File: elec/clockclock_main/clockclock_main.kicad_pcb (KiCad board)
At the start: 2 copper layers, 226.2 x 90.5 mm, 132 parts, among them J1 rotary_encoder, J2 DCF77 board, J3 RTC, J4 rotary_encoder, M1 Conn motor 0, M10 Conn motor 1, M11 Conn motor 0, M12 Conn motor 1, M13 Conn motor 0, M14 Conn motor 1, M15 Conn motor 0, M16 Conn motor 1, M17 Conn motor 0, M18 Conn motor 1, M19 Conn motor 0, M2 Conn motor 1, M20 Conn motor 1, M21 Conn motor 0, M22 Conn motor 1, M23 Conn motor 0, M24 Conn motor 1, M3 Conn motor 0, M4 Conn motor 1, M5 Conn motor 0, M6 Conn motor 1, M7 Conn motor 0, M8 Conn motor 1, M9 Conn motor 0, U1 ESP32-C3-DEVKITM-1, U10 VID6606, U11 74HCT595, U12 VID6606, U13 74HCT595, U14 VID6606, U15 74HCT595, U16 VID6606, U17 74HCT595, U18 VID6606, U19 74HCT595, U2 TXB0102DCT, U20 VID6606, U21 74HCT595, U22 VID6606, U23 74HCT595, U24 VID6606, U25 74HCT595, U26 VID6606, U3 74HCT595, U4 VID6606, U5 74HCT595, U6 VID6606, U7 74HCT595, U8 VID6606, U9 74HCT595

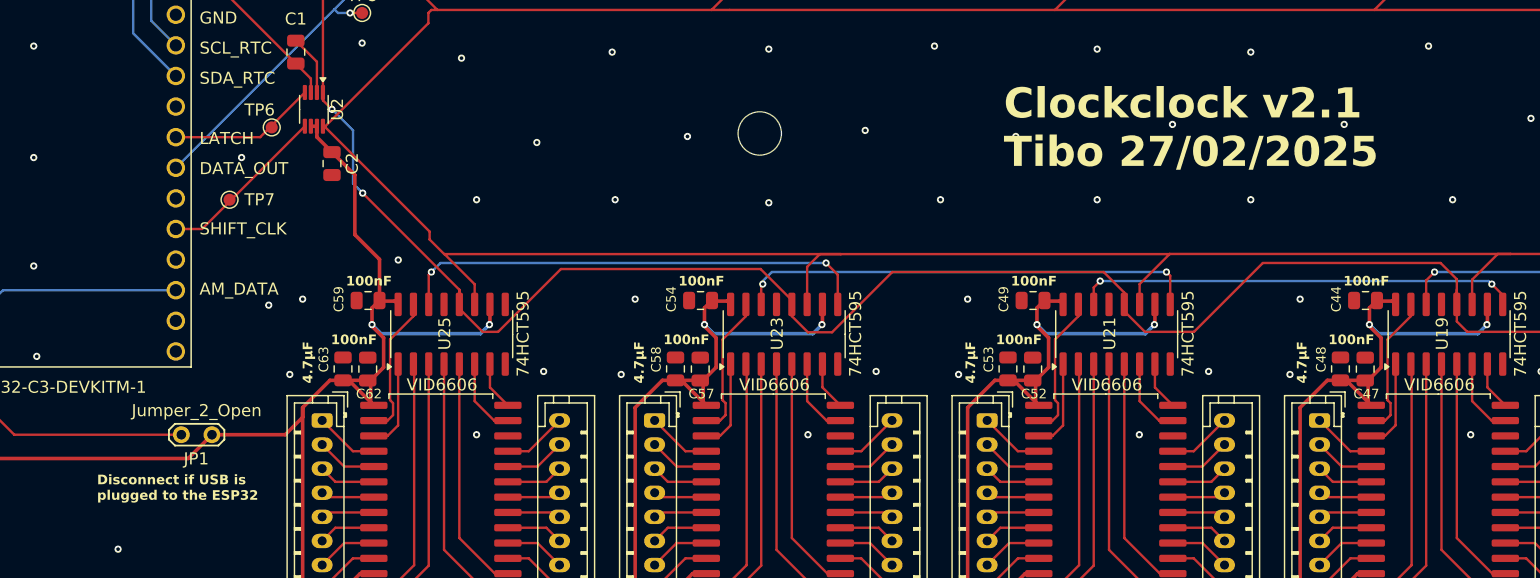
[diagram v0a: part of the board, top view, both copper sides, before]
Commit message: [elec] Update silkscreen for USB power
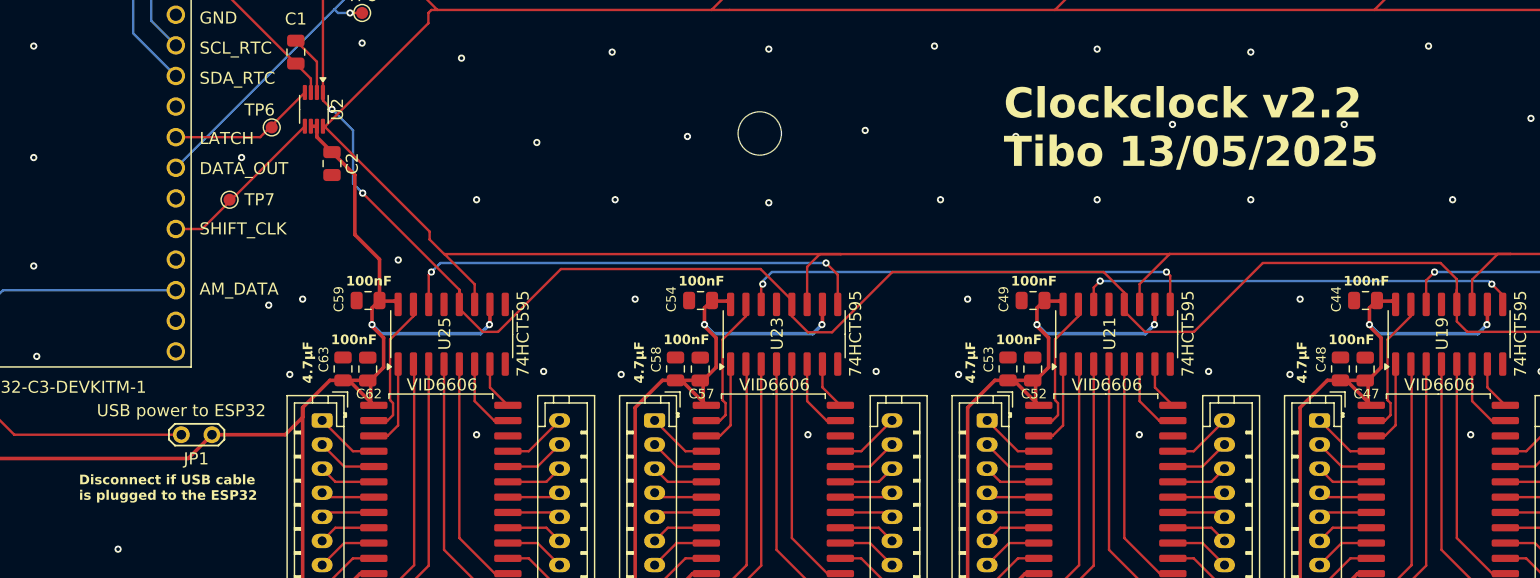
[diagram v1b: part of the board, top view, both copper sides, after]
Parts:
- JP1: value Jumper_2_Open -> USB power to ESP32
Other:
- board text added: "Clockclock v2.2 Tibo 13/05/2025"
- board text added: "Disconnect if USB cable is plugged to the ESP32"
- board text removed: "Clockclock v2.1 Tibo 27/02/2025"
- board text removed: "Disconnect if USB is plugged to the ESP32"
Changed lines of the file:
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@@
 			)
 		)
-		(property "Value" "Jumper_2_Open"
-			(at 1.27 2 0)
+		(property "Value" "USB power to ESP32"
+			(at 2.54 2 0)
 			(layer "F.SilkS")
 			(effects
@@
 		)
 	)
-	(gr_text "Disconnect if USB is\nplugged to the ESP32"
-		(at 75 115.5 0)
+	(gr_text "Disconnect if USB cable\nis plugged to the ESP32"
+		(at 73.5 115.5 0)
 		(layer "F.SilkS")
 		(effects
@@
 		)
 	)
-	(gr_text "Clockclock v2.1\nTibo 27/02/2025"
+	(gr_text "Clockclock v2.2\nTibo 13/05/2025"
 		(at 150.25 88 0)
 		(layer "F.SilkS")
